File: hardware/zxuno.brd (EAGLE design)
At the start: 86 x 56 mm, 103 parts, among them T1 BC846, U1 6SLX9TQG144, U2 FLASH-SPI-25XXSMD1, U4 AD724, U5 50MHz, U6 3.3V, U7 1.2V, Y1 3.58M, Y2 4.43M

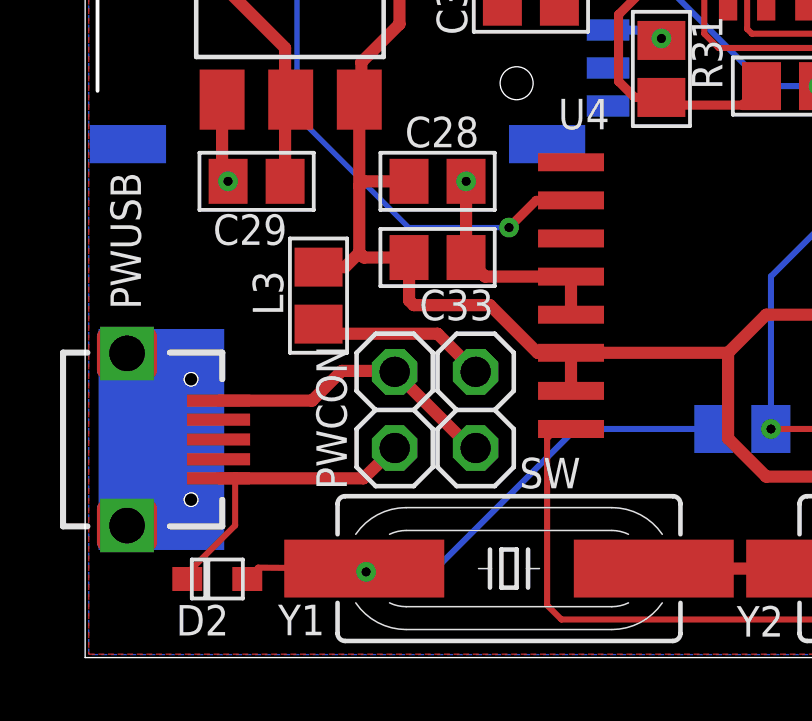
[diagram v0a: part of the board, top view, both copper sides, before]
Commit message: Añado pines de datos al conector microUSB
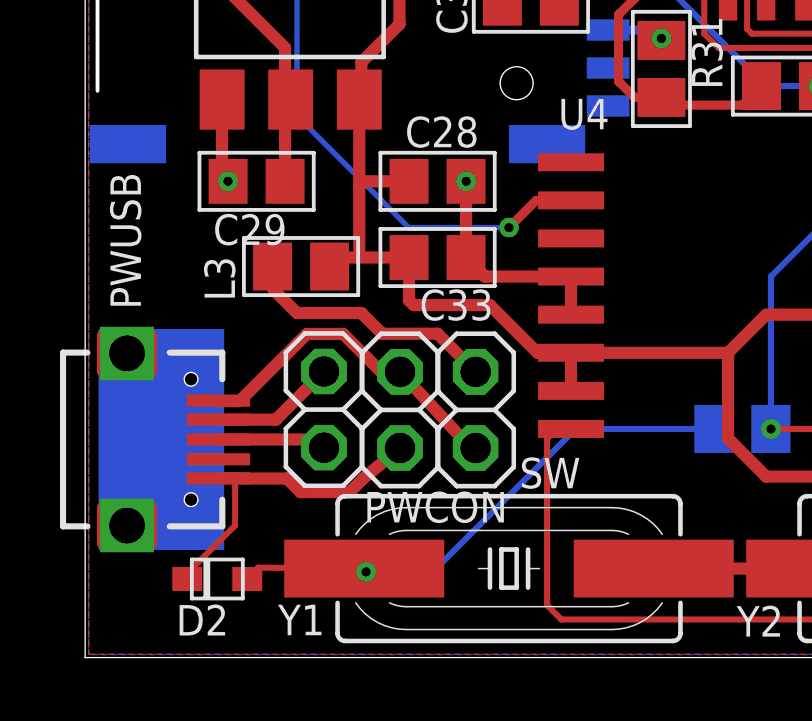
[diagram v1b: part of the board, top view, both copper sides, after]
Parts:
- added DATA: (no value), pinhead:1X02
- moved L3 1.13 mm to (7.20, 13.0), turned to 0 degrees
- moved PWCON 0.18 mm to (10.5, 8.26)
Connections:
- new net N$16: DATA.1, PWUSB.2
- new net N$29: DATA.2, PWUSB.3
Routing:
- net N$16: track 0.00 -> 4.18 mm
- net N$29: track 0.00 -> 3.63 mm
- net N$13: track 5.90 -> 8.65 mm
- net N$12: track 10.1 -> 11.1 mm
- net GND: track 149.1 -> 149.7 mm
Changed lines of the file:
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@@
 <text x="3.0916625" y="27.65549375" size="1.016" layer="125" font="vector" ratio="15">L1</text>
 <text x="21.55825" y="30.8014625" size="1.016" layer="125" font="vector" ratio="15" rot="R90">L2</text>
-<text x="5.588" y="12.898425" size="1.016" layer="125" font="vector" ratio="15" rot="R270">L3</text>
+<text x="3.9864375" y="13.3593625" size="1.016" layer="125" font="vector" ratio="15" rot="R270">L3</text>
 <text x="73.174734375" y="1.7787125" size="1.016" layer="125" font="vector" ratio="15" rot="SR0">PS/2</text>
-<text x="8.722690625" y="5.596484375" size="1.016" layer="125" font="vector" ratio="15" rot="R90">PWCON</text>
+<text x="9.283984375" y="4.496059375" size="1.016" layer="125" font="vector" ratio="15">PWCON</text>
 <text x="1.859509375" y="11.6053375" size="1.016" layer="125" font="vector" ratio="15" rot="SR90">PWUSB</text>
 <text x="41.2115" y="9.81075" size="1.016" layer="125" font="vector" ratio="15">R1</text>
@@
 <attribute name="VALUE" x="22.225" y="16.51" size="1.27" layer="27"/>
 </element>
-<element name="L3" library="rcl" package="M0805" value="" x="7.77875" y="12.065" smashed="yes" rot="R90">
-<attribute name="NAME" x="5.588" y="12.8984375" size="1.016" layer="25" font="vector" ratio="15" rot="R270"/>
-<attribute name="VALUE" x="10.31875" y="10.795" size="1.27" layer="27" rot="R90"/>
+<element name="L3" library="rcl" package="M0805" value="" x="7.1978125" y="13.03375" smashed="yes">
+<attribute name="NAME" x="3.978625" y="13.375" size="1.016" layer="25" font="vector" ratio="15" rot="R270"/>
+<attribute name="VALUE" x="5.9278125" y="10.49375" size="1.27" layer="27"/>
 </element>
 <element name="U6" library="burr-brown" package="SOT223" value="3.3V" x="6.82625" y="21.74875" smashed="yes">
@@
 <attribute name="VALUE" x="9.8425" y="10.795" size="1.27" layer="27" rot="R270"/>
 </element>
-<element name="PWCON" library="pinhead" package="1X02" value="" x="10.31875" y="8.255" smashed="yes" rot="R90">
-<attribute name="NAME" x="8.722690625" y="5.59648125" size="1.016" layer="25" font="vector" ratio="15" rot="R90"/>
-<attribute name="VALUE" x="13.49375" y="5.715" size="1.27" layer="27" rot="R90"/>
+<element name="PWCON" library="pinhead" package="1X02" value="" x="10.4984375" y="8.255" smashed="yes" rot="R90">
+<attribute name="NAME" x="9.28398125" y="4.503871875" size="1.016" layer="25" font="vector" ratio="15"/>
+<attribute name="VALUE" x="13.6734375" y="5.715" size="1.27" layer="27" rot="R90"/>
 </element>
 <element name="PS/2" library="ZX_UNO_0_14" package="DINC/MIN_TM/6_1PRIMARY" value="PS/2 Keyb" x="85.56625" y="10.16" smashed="yes" rot="R270">
@@
 <element name="CVBS" library="uzebox" package="RCA" value="RCA" x="46.2046875" y="50.8" smashed="yes">
 <attribute name="NAME" x="40.86671875" y="45.7596875" size="1.016" layer="25" font="vector" ratio="15" rot="R180"/>
+</element>
+<element name="DATA" library="pinhead" package="1X02" value="" x="7.9609375" y="8.265625" smashed="yes" rot="R270">
+<attribute name="NAME" x="5.7897375" y="10.33495" size="1.015" layer="125" font="vector" ratio="15" rot="R270"/>
+<attribute name="VALUE" x="4.7859375" y="10.805625" size="1.27" layer="27" rot="R270"/>
 </element>
 </elements>
@@
 <contactref element="SDCARD" pad="M2"/>
 <contactref element="JTAG" pad="2"/>
-<wire x1="10.31875" y1="6.985" x2="10.31875" y2="6.9453125" width="0.4064" layer="1"/>
+<wire x1="10.4984375" y1="6.985" x2="10.31875" y2="6.9453125" width="0.4064" layer="1"/>
 <wire x1="4.445" y1="5.97485" x2="5.000625" y2="5.97485" width="0.4064" layer="1"/>
-<wire x1="5.000625" y1="5.97485" x2="9.27735" y2="5.97485" width="0.4064" layer="1"/>
-<wire x1="9.27735" y1="5.97485" x2="10.31875" y2="6.985" width="0.4064" layer="1"/>
+<wire x1="9.27735" y1="5.97485" x2="10.4984375" y2="6.985" width="0.4064" layer="1"/>
 <wire x1="3.4053125" y1="2.619375" x2="3.4053125" y2="2.81" width="0.2032" layer="1"/>
 <wire x1="3.4053125" y1="2.81" x2="5.000625" y2="4.4053125" width="0.2032" layer="1"/>
@@
 <wire x1="53.75671875" y1="35.06390625" x2="52.85859375" y2="35.06390625" width="0.1778" layer="1"/>
 <wire x1="52.85859375" y1="35.06390625" x2="52.85125" y2="35.07125" width="0.1778" layer="1"/>
+<wire x1="9.27735" y1="5.97485" x2="9.27735" y2="5.9726625" width="0.4064" layer="1"/>
+<wire x1="9.27735" y1="5.9726625" x2="8.8203125" y2="5.515625" width="0.4064" layer="1"/>
+<wire x1="8.8203125" y1="5.515625" x2="7.1796875" y2="5.515625" width="0.4064" layer="1"/>
+<wire x1="7.1796875" y1="5.515625" x2="6.7265625" y2="5.96875" width="0.4064" layer="1"/>
+<wire x1="6.7265625" y1="5.96875" x2="5.006725" y2="5.96875" width="0.4064" layer="1"/>
+<wire x1="5.006725" y1="5.96875" x2="5.000625" y2="5.97485" width="0.4064" layer="1"/>
 </signal>
 <signal name="XD0">
@@
 <contactref element="SW" pad="2"/>
 <wire x1="13.0175" y1="6.985" x2="12.85875" y2="6.985" width="0.4064" layer="1"/>
-<wire x1="12.85875" y1="6.985" x2="10.31875" y2="9.525" width="0.4064" layer="1"/>
+<wire x1="12.85875" y1="6.985" x2="10.4984375" y2="9.525" width="0.4064" layer="1"/>
 <contactref element="PWUSB" pad="1"/>
-<wire x1="4.445" y1="8.56565" x2="7.565275" y2="8.56565" width="0.4064" layer="1"/>
-<wire x1="7.565275" y1="8.56565" x2="8.555875" y2="9.55625" width="0.4064" layer="1"/>
-<wire x1="8.555875" y1="9.55625" x2="10.31875" y2="9.55625" width="0.4064" layer="1"/>
-<wire x1="10.31875" y1="9.55625" x2="10.31875" y2="9.525" width="0.4064" layer="1"/>
+<wire x1="10.31875" y1="9.55625" x2="10.4984375" y2="9.525" width="0.4064" layer="1"/>
+<wire x1="10.31875" y1="9.55625" x2="9.834375" y2="9.55625" width="0.4064" layer="1"/>
+<wire x1="9.834375" y1="9.55625" x2="8.6015625" y2="10.7890625" width="0.4064" layer="1"/>
+<wire x1="8.6015625" y1="10.7890625" x2="7.390625" y2="10.7890625" width="0.4064" layer="1"/>
+<wire x1="7.390625" y1="10.7890625" x2="5.1484375" y2="8.546875" width="0.4064" layer="1"/>
+<wire x1="5.1484375" y1="8.546875" x2="4.463775" y2="8.546875" width="0.4064" layer="1"/>
+<wire x1="4.463775" y1="8.546875" x2="4.445" y2="8.56565" width="0.4064" layer="1"/>
 </signal>
 <signal name="N$13">
@@
 <contactref element="SW" pad="1"/>
 <wire x1="13.0175" y1="9.525" x2="11.7475" y2="10.795" width="0.4064" layer="1"/>
-<wire x1="11.7475" y1="10.795" x2="8.09875" y2="10.795" width="0.4064" layer="1"/>
-<wire x1="8.09875" y1="10.795" x2="7.77875" y2="11.115" width="0.4064" layer="1"/>
+<wire x1="11.7475" y1="10.795" x2="9.9003125" y2="10.795" width="0.4064" layer="1"/>
+<wire x1="9.9003125" y1="10.795" x2="9.2109375" y2="11.484375" width="0.4064" layer="1"/>
+<wire x1="9.2109375" y1="11.484375" x2="7.0625" y2="11.484375" width="0.4064" layer="1"/>
+<wire x1="7.0625" y1="11.484375" x2="6.2734375" y2="12.2734375" width="0.4064" layer="1"/>
+<wire x1="6.2734375" y1="12.2734375" x2="6.2734375" y2="13.008125" width="0.4064" layer="1"/>
+<wire x1="6.2734375" y1="13.008125" x2="6.2478125" y2="13.03375" width="0.4064" layer="1"/>
 </signal>
 <signal name="5V">
@@
 <wire x1="10.7975" y1="11.90375" x2="10.95375" y2="11.7475" width="0.4064" layer="1"/>
 <wire x1="9.13765" y1="18.59915" x2="9.13765" y2="15.71625" width="0.4064" layer="1"/>
-<wire x1="9.13765" y1="15.71625" x2="9.13765" y2="13.49375" width="0.4064" layer="1"/>
+<wire x1="9.13765" y1="15.71625" x2="9.13765" y2="13.3867125" width="0.4064" layer="1"/>
 <wire x1="10.7975" y1="15.875" x2="9.2964" y2="15.875" width="0.4064" layer="1"/>
 <wire x1="9.2964" y1="15.875" x2="9.13765" y2="15.71625" width="0.4064" layer="1"/>
-<wire x1="10.7975" y1="13.335" x2="9.2964" y2="13.335" width="0.4064" layer="1"/>
-<wire x1="9.2964" y1="13.335" x2="9.13765" y2="13.49375" width="0.4064" layer="1"/>
-<wire x1="7.77875" y1="13.015" x2="8.6589" y2="13.015" width="0.4064" layer="1"/>
-<wire x1="8.6589" y1="13.015" x2="9.13765" y2="13.49375" width="0.4064" layer="1"/>
 <wire x1="30.31875" y1="7.46125" x2="30.31875" y2="6.9825" width="0.2032" layer="1"/>
 <wire x1="24.4475" y1="11.43" x2="25.39625" y2="11.43" width="0.2032" layer="1"/>
@@
 <wire x1="47.5853125" y1="43.6959375" x2="39.3620625" y2="43.6959375" width="0.3048" layer="16"/>
 <wire x1="39.3620625" y1="43.6959375" x2="33.147" y2="49.911" width="0.3048" layer="16"/>
+<wire x1="8.1478125" y1="13.03375" x2="8.1478125" y2="13.2103125" width="0.4064" layer="1"/>
+<wire x1="8.1478125" y1="13.2103125" x2="8.2734375" y2="13.3359375" width="0.4064" layer="1"/>
+<wire x1="10.7975" y1="13.335" x2="9.0859375" y2="13.335" width="0.4064" layer="1"/>
+<wire x1="9.0859375" y1="13.335" x2="8.4490625" y2="13.335" width="0.4064" layer="1"/>
+<wire x1="8.4490625" y1="13.335" x2="8.1478125" y2="13.03375" width="0.4064" layer="1"/>
+<wire x1="9.13765" y1="13.3867125" x2="9.0859375" y2="13.335" width="0.4064" layer="1"/>
 </signal>
 <signal name="N$14">
@@
 <wire x1="74.77125" y1="16.03375" x2="70.96125" y2="16.03375" width="0.1778" layer="1"/>
 </signal>
+<signal name="N$16">
+<contactref element="PWUSB" pad="2"/>
+<contactref element="DATA" pad="1"/>
+<wire x1="6.3559625" y1="7.93065" x2="7.9609375" y2="9.535625" width="0.4064" layer="1"/>
+<wire x1="6.3559625" y1="7.93065" x2="4.445" y2="7.93065" width="0.4064" layer="1"/>
+</signal>
+<signal name="N$29">
+<contactref element="PWUSB" pad="3"/>
+<contactref element="DATA" pad="2"/>
+<wire x1="7.6863125" y1="7.27025" x2="7.9609375" y2="6.995625" width="0.4064" layer="1"/>
+<wire x1="7.6863125" y1="7.27025" x2="4.445" y2="7.27025" width="0.4064" layer="1"/>
+</signal>
 </signals>

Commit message: Añado USB Blaster en plan addon
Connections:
- net N$16 renamed D-
- net N$29 renamed D+
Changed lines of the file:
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@@
 <wire x1="74.77125" y1="16.03375" x2="70.96125" y2="16.03375" width="0.1778" layer="1"/>
 </signal>
-<signal name="N$16">
+<signal name="D-">
 <contactref element="PWUSB" pad="2"/>
 <contactref element="DATA" pad="1"/>
@@
 <wire x1="6.3559625" y1="7.93065" x2="4.445" y2="7.93065" width="0.4064" layer="1"/>
 </signal>
-<signal name="N$29">
+<signal name="D+">
 <contactref element="PWUSB" pad="3"/>
 <contactref element="DATA" pad="2"/>

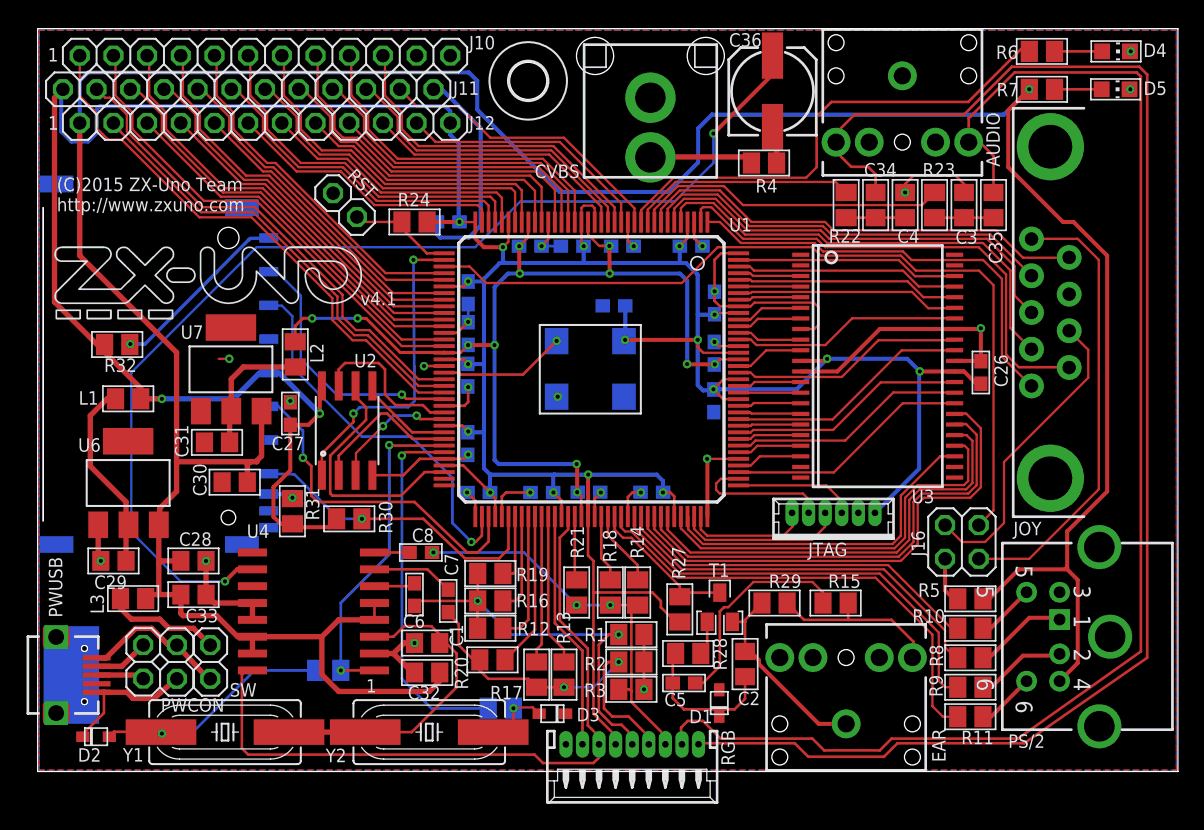
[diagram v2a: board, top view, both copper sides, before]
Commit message: Quito pines de datos del microUSB, cambio JTAG a 2.54mm y pongo pines teclado con 5V
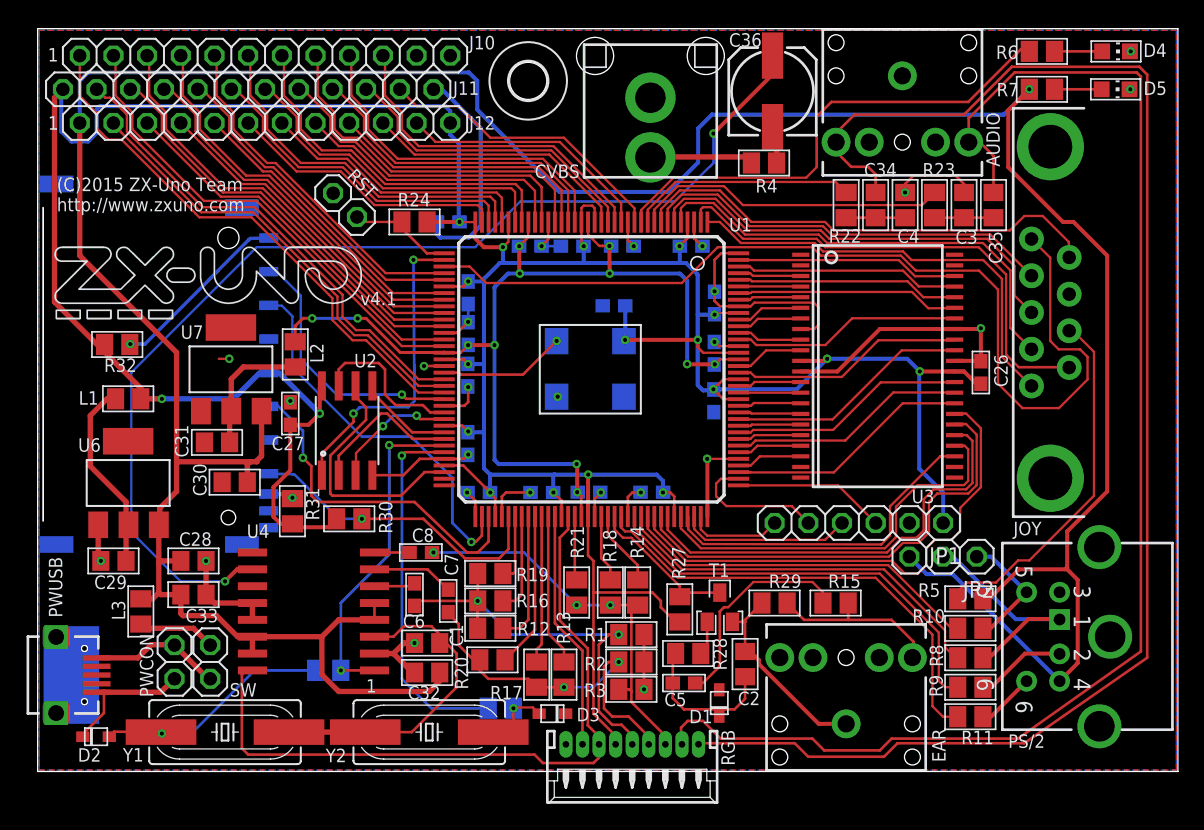
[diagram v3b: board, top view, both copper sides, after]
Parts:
- removed DATA: (no value), pinhead:1X02
- removed J16: (no value), pinhead:2X02
- removed JTAG: JTAG, con-molex:53047-06
- added JP1: (no value), pinhead:1X06
- added JP2: (no value), pinhead:1X03
- moved L3 1.13 mm to (7.78, 12.1), turned to 90 degrees
- moved PWCON 0.18 mm to (10.3, 8.26)
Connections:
- removed net D+: DATA.2, PWUSB.3
- removed net D-: DATA.1, PWUSB.2
- removed net N$2: PS/2.5, R10.1
- removed net N$4: PS/2.1, R8.1
- removed net PIN5: J16.2, JOY.5
- removed net PIN7: J16.3, JOY.7
- new net CLKPS2: JP2.1, PS/2.5, R10.1
- new net DATAPS2: JP2.2, PS/2.1, R8.1
- net 3.3V: now also JP1.1; no longer JTAG.1
- net 5V: now also JP2.3
- net GND: now also JP1.2; no longer JTAG.2
- net JOY_FIRE3: now also JOY.5; no longer J16.1
- net N$15: now also JOY.7; no longer J16.4
- net TCK: now also JP1.3; no longer JTAG.3
- net TDI: now also JP1.5; no longer JTAG.5
- net TDO: now also JP1.4; no longer JTAG.4
- net TMS: now also JP1.6; no longer JTAG.6
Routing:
- net PIN5: track 34.3 -> 0.00 mm
- net N$15: track 3.60 -> 27.2 mm
- net PIN7: track 23.3 -> 0.00 mm
- net DATAPS2: track 0.00 -> 17.8 mm
- net 5V: track 233.4 -> 248.1 mm
- net JOY_FIRE3: track 62.8 -> 73.5 mm
- net CLKPS2: track 0.00 -> 9.29 mm
- net N$4: track 7.09 -> 0.00 mm
- net N$2: track 4.42 -> 0.00 mm
- net D-: track 4.18 -> 0.00 mm
- net D+: track 3.63 -> 0.00 mm
- net N$13: track 8.65 -> 5.90 mm
- net TCK: track 9.17 -> 11.5 mm
- net TMS: track 9.41 -> 7.13 mm
- net JOY_FIRE2: track 34.5 -> 36.0 mm
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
